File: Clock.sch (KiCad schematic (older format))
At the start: 4 parts, among them Y1 24 MHz

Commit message: First pass at pcb layout
Not really ready to set that in stone, but wanted to get an idea of what size enclosure will work.
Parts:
- C30, C31: footprint (none) -> Capacitor_SMD:C_1210_3225Metric
- R14: footprint (none) -> Resistor_SMD:R_1210_3225Metric
- Y1: footprint (none) -> Crystal:Crystal_SMD_SeikoEpson_MA505-2Pin_12.7x5.1mm
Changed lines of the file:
@@
 $Descr A4 11693 8268
 encoding utf-8
-Sheet 6 6
+Sheet 5 6
 Title ""
 Date ""
@@
 $EndDescr
 $Comp
-L power:GNDREF #PWR?
+L power:GNDREF #PWR0117
 U 1 1 604F5E86
 P 5800 4950
-F 0 "#PWR?" H 5800 4700 50  0001 C CNN
+F 0 "#PWR0117" H 5800 4700 50  0001 C CNN
 F 1 "GNDREF" H 5805 4777 50  0000 C CNN
 F 2 "" H 5800 4950 50  0001 C CNN
@@
 F 0 "C30" H 5515 4596 50  0000 L CNN
 F 1 "18 pF" H 5515 4505 50  0000 L CNN
-F 2 "" H 5438 4400 50  0001 C CNN
+F 2 "Capacitor_SMD:C_1210_3225Metric" H 5438 4400 50  0001 C CNN
 F 3 "~" H 5400 4550 50  0001 C CNN
 	1    5400 4550
@@
 F 0 "C31" H 6265 4596 50  0000 L CNN
 F 1 "18 pF" H 6265 4505 50  0000 L CNN
-F 2 "" H 6188 4400 50  0001 C CNN
+F 2 "Capacitor_SMD:C_1210_3225Metric" H 6188 4400 50  0001 C CNN
 F 3 "~" H 6150 4550 50  0001 C CNN
 	1    6150 4550
@@
 F 0 "Y1" H 5800 4318 50  0000 C CNN
 F 1 "24 MHz" H 5800 4227 50  0000 C CNN
-F 2 "" H 5800 4050 50  0001 C CNN
+F 2 "Crystal:Crystal_SMD_SeikoEpson_MA505-2Pin_12.7x5.1mm" H 5800 4050 50  0001 C CNN
 F 3 "~" H 5800 4050 50  0001 C CNN
 	1    5800 4050
@@
 F 0 "R14" V 5593 3450 50  0000 C CNN
 F 1 "1 MΩ" V 5684 3450 50  0000 C CNN
-F 2 "" V 5730 3450 50  0001 C CNN
+F 2 "Resistor_SMD:R_1210_3225Metric" V 5730 3450 50  0001 C CNN
 F 3 "~" H 5800 3450 50  0001 C CNN
 	1    5800 3450

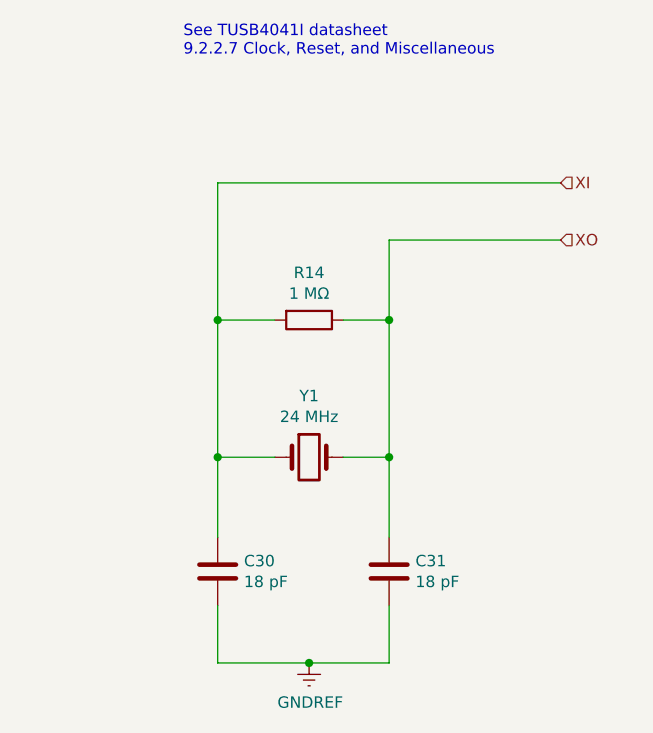
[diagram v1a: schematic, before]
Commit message: Swap TUSB4041I for TUSB2036
The 4041 does more than I need it to, so use the 2036 instead.
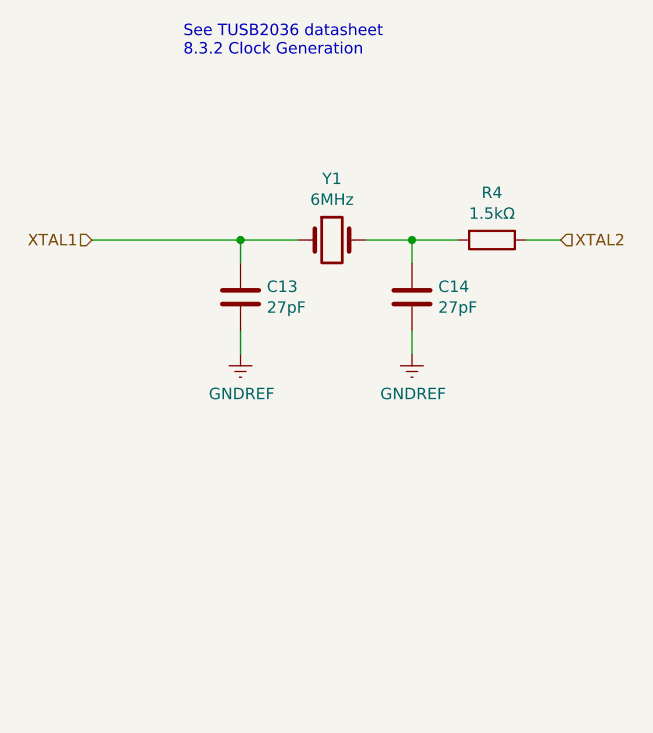
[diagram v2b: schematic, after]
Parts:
- removed C30, C31: 18 pF, Capacitor_SMD:C_1210_3225Metric, symbol Device:C
- removed R14: 1 MΩ, Resistor_SMD:R_1210_3225Metric, symbol Device:R
- added C13, C14: 27pF, Capacitor_SMD:C_1210_3225Metric, symbol Device:C
- added R4: 1.5kΩ, Resistor_SMD:R_1210_3225Metric, symbol Device:R
- Y1: value 24 MHz -> 6MHz; footprint Crystal:Crystal_SMD_SeikoEpson_MA505-2Pin_12.7x5.1mm -> Crystal:Crystal_DS26_D2.0mm_L6.0mm_Horizontal
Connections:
- net GNDREF: now also C13.2, C14.2
- net XI renamed XTAL1
- net XTAL1: now also C13.1
- net XO: no longer names the net of Y1.2
- net XO: now also C14.1, R4.2
- new net XTAL2: R4.1
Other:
- note added: "See TUSB2036 datasheet\n8.3.2 Clock Generation"
- note removed: "See TUSB4041I datasheet\n9.2.2.7 Clock, Reset, and Miscellaneous"
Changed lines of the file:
@@
 $Descr A4 11693 8268
 encoding utf-8
-Sheet 5 6
+Sheet 4 6
 Title ""
 Date ""
@@
 Comment4 ""
 $EndDescr
+Text HLabel 4850 3100 0    50   Input ~ 0
+XTAL1
+Text HLabel 6900 3100 2    50   Input ~ 0
+XTAL2
+Text Notes 5250 2300 0    50   ~ 0
+See TUSB2036 datasheet\n8.3.2 Clock Generation
 $Comp
-L power:GNDREF #PWR0117
-U 1 1 604F5E86
-P 5800 4950
-F 0 "#PWR0117" H 5800 4700 50  0001 C CNN
-F 1 "GNDREF" H 5805 4777 50  0000 C CNN
-F 2 "" H 5800 4950 50  0001 C CNN
-F 3 "" H 5800 4950 50  0001 C CNN
-	1    5800 4950
+L Device:Crystal Y1
+U 1 1 604F9C8F
+P 5900 3100
+F 0 "Y1" H 5900 3368 50  0000 C CNN
+F 1 "6MHz" H 5900 3277 50  0000 C CNN
+F 2 "Crystal:Crystal_DS26_D2.0mm_L6.0mm_Horizontal" H 5900 3100 50  0001 C CNN
+F 3 "~" H 5900 3100 50  0001 C CNN
+	1    5900 3100
+	1    0    0    -1
+$EndComp
+Wire Wire Line
+	4850 3100 5500 3100
+Wire Wire Line
+	6050 3100 6250 3100
+$Comp
+L Device:R R4
+U 1 1 604FA19F
+P 6600 3100
+F 0 "R4" V 6393 3100 50  0000 C CNN
+F 1 "1.5kΩ" V 6484 3100 50  0000 C CNN
+F 2 "Resistor_SMD:R_1210_3225Metric" V 6530 3100 50  0001 C CNN
+F 3 "~" H 6600 3100 50  0001 C CNN
+	1    6600 3100
+	0    1    1    0
+$EndComp
+Wire Wire Line
+	6750 3100 6900 3100
+$Comp
+L Device:C C14
+U 1 1 604FA65B
+P 6250 3350
+F 0 "C14" H 6365 3396 50  0000 L CNN
+F 1 "27pF" H 6365 3305 50  0000 L CNN
+F 2 "Capacitor_SMD:C_1210_3225Metric" H 6288 3200 50  0001 C CNN
+F 3 "~" H 6250 3350 50  0001 C CNN
+	1    6250 3350
 	1    0    0    -1
 $EndComp
 $Comp
-L Device:C C30
-U 1 1 604F6174
-P 5400 4550
-F 0 "C30" H 5515 4596 50  0000 L CNN
-F 1 "18 pF" H 5515 4505 50  0000 L CNN
-F 2 "Capacitor_SMD:C_1210_3225Metric" H 5438 4400 50  0001 C CNN
-F 3 "~" H 5400 4550 50  0001 C CNN
-	1    5400 4550
+L Device:C C13
+U 1 1 604FA9C5
+P 5500 3350
+F 0 "C13" H 5615 3396 50  0000 L CNN
+F 1 "27pF" H 5615 3305 50  0000 L CNN
+F 2 "Capacitor_SMD:C_1210_3225Metric" H 5538 3200 50  0001 C CNN
+F 3 "~" H 5500 3350 50  0001 C CNN
+	1    5500 3350
 	1    0    0    -1
 $EndComp
 $Comp
-L Device:C C31
-U 1 1 604F6998
-P 6150 4550
-F 0 "C31" H 6265 4596 50  0000 L CNN
-F 1 "18 pF" H 6265 4505 50  0000 L CNN
-F 2 "Capacitor_SMD:C_1210_3225Metric" H 6188 4400 50  0001 C CNN
-F 3 "~" H 6150 4550 50  0001 C CNN
-	1    6150 4550
+L power:GNDREF #PWR0135
+U 1 1 604FAB4A
+P 5500 3600
+F 0 "#PWR0135" H 5500 3350 50  0001 C CNN
+F 1 "GNDREF" H 5505 3427 50  0000 C CNN
+F 2 "" H 5500 3600 50  0001 C CNN
+F 3 "" H 5500 3600 50  0001 C CNN
+	1    5500 3600
 	1    0    0    -1
 $EndComp
 $Comp
-L Device:Crystal Y1
-U 1 1 604F8137
-P 5800 4050
-F 0 "Y1" H 5800 4318 50  0000 C CNN
-F 1 "24 MHz" H 5800 4227 50  0000 C CNN
-F 2 "Crystal:Crystal_SMD_SeikoEpson_MA505-2Pin_12.7x5.1mm" H 5800 4050 50  0001 C CNN
-F 3 "~" H 5800 4050 50  0001 C CNN
-	1    5800 4050
+L power:GNDREF #PWR0136
+U 1 1 604FADB7
+P 6250 3600
+F 0 "#PWR0136" H 6250 3350 50  0001 C CNN
+F 1 "GNDREF" H 6255 3427 50  0000 C CNN
+F 2 "" H 6250 3600 50  0001 C CNN
+F 3 "" H 6250 3600 50  0001 C CNN
+	1    6250 3600
 	1    0    0    -1
 $EndComp
-$Comp
-L Device:R R14
-U 1 1 604F8499
-P 5800 3450
-F 0 "R14" V 5593 3450 50  0000 C CNN
-F 1 "1 MΩ" V 5684 3450 50  0000 C CNN
-F 2 "Resistor_SMD:R_1210_3225Metric" V 5730 3450 50  0001 C CNN
-F 3 "~" H 5800 3450 50  0001 C CNN
-	1    5800 3450
-	0    1    1    0
-$EndComp
-Text HLabel 6900 2850 2    50   Input ~ 0
-XI
-Text HLabel 6900 3100 2    50   Input ~ 0
-XO
 Wire Wire Line
-	6900 2850 5400 2850
+	5500 3200 5500 3100
+Connection ~ 5500 3100
 Wire Wire Line
-	5400 2850 5400 3450
+	5500 3100 5750 3100
 Wire Wire Line
-	5650 3450 5400 3450
-Connection ~ 5400 3450
+	6250 3200 6250 3100
+Connection ~ 6250 3100
 Wire Wire Line
-	5400 3450 5400 4050
+	6250 3100 6450 3100
 Wire Wire Line
-	5650 4050 5400 4050
-Connection ~ 5400 4050
+	5500 3500 5500 3600
 Wire Wire Line
-	5400 4050 5400 4400
-Wire Wire Line
-	6900 3100 6150 3100
-Wire Wire Line
-	6150 3100 6150 3450
-Wire Wire Line
-	5950 3450 6150 3450
-Connection ~ 6150 3450
-Wire Wire Line
-	6150 3450 6150 4050
-Wire Wire Line
-	5950 4050 6150 4050
-Connection ~ 6150 4050
-Wire Wire Line
-	6150 4050 6150 4400
-Wire Wire Line
-	5400 4700 5400 4950
-Wire Wire Line
-	5400 4950 5800 4950
-Wire Wire Line
-	6150 4700 6150 4950
-Wire Wire Line
-	6150 4950 5800 4950
-Connection ~ 5800 4950
-Text Notes 5250 2300 0    50   ~ 0
-See TUSB4041I datasheet\n9.2.2.7 Clock, Reset, and Miscellaneous
+	6250 3500 6250 3600
 $EndSCHEMATC

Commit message: Add BOM and clarify some footprints
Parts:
- C13, C14: Manufacturer_Name (none) -> AVX; Manufacturer_Part_Number (none) -> 12102U270JAT2A; Price (none) -> 0.7; Vendor (none) -> Mouser; Vendor Part Number (none) -> 581-12102U270JAT2A
- R4: Manufacturer_Name (none) -> Yageo; Manufacturer_Part_Number (none) -> AC1210FR-071K5L; Price (none) -> 0.31; Vendor (none) -> Mouser; Vendor Part Number (none) -> 603-AC1210FR-071K5L
- Y1: footprint Crystal:Crystal_DS26_D2.0mm_L6.0mm_Horizontal -> Crystal:Crystal_SMD_Abracon_ABM7-2Pin_6.0x3.5mm; Description (none) -> Hub controller clock; Manufacturer_Name (none) -> ABRACON; Manufacturer_Part_Number (none) -> AWSCR-6.00CPLA-C30-T4; Price (none) -> 0.36; Vendor (none) -> Mouser; Vendor Part Number (none) -> 815-CR-6.00CPLA-30-T
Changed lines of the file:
@@
 Comment4 ""
 $EndDescr
-Text HLabel 4850 3100 0    50   Input ~ 0
-XTAL1
-Text HLabel 6900 3100 2    50   Input ~ 0
-XTAL2
-Text Notes 5250 2300 0    50   ~ 0
-See TUSB2036 datasheet\n8.3.2 Clock Generation
 $Comp
 L Device:Crystal Y1
@@
 F 0 "Y1" H 5900 3368 50  0000 C CNN
 F 1 "6MHz" H 5900 3277 50  0000 C CNN
-F 2 "Crystal:Crystal_DS26_D2.0mm_L6.0mm_Horizontal" H 5900 3100 50  0001 C CNN
-F 3 "~" H 5900 3100 50  0001 C CNN
+F 2 "Crystal:Crystal_SMD_Abracon_ABM7-2Pin_6.0x3.5mm" H 5900 3100 50  0001 C CNN
+F 3 "https://www.mouser.com/datasheet/2/3/AWSCR-CPLA-1595603.pdf" H 5900 3100 50  0001 C CNN
+F 4 "Hub controller clock" H 5900 3468 50  0001 C CNN "Description"
+F 5 "ABRACON" H 5900 3468 50  0001 C CNN "Manufacturer_Name"
+F 6 "AWSCR-6.00CPLA-C30-T4" H 5900 3468 50  0001 C CNN "Manufacturer_Part_Number"
+F 7 "0.36" H 5900 3468 50  0001 C CNN "Price"
+F 8 "815-CR-6.00CPLA-30-T" H 5900 3468 50  0001 C CNN "Vendor Part Number"
+F 9 "Mouser" H 5900 3468 50  0001 C CNN "Vendor"
 	1    5900 3100
 	1    0    0    -1
 $EndComp
-Wire Wire Line
-	4850 3100 5500 3100
-Wire Wire Line
-	6050 3100 6250 3100
 $Comp
 L Device:R R4
@@
 F 1 "1.5kΩ" V 6484 3100 50  0000 C CNN
 F 2 "Resistor_SMD:R_1210_3225Metric" V 6530 3100 50  0001 C CNN
-F 3 "~" H 6600 3100 50  0001 C CNN
+F 3 "https://www.mouser.com/datasheet/2/447/PYu_AC_51_RoHS_L_7-1714230.pdf" H 6600 3100 50  0001 C CNN
+F 4 "Yageo" H 6393 3200 50  0001 C CNN "Manufacturer_Name"
+F 5 "AC1210FR-071K5L" H 6393 3200 50  0001 C CNN "Manufacturer_Part_Number"
+F 6 "0.31" H 6393 3200 50  0001 C CNN "Price"
+F 7 "603-AC1210FR-071K5L" H 6393 3200 50  0001 C CNN "Vendor Part Number"
+F 8 "Mouser" H 6393 3200 50  0001 C CNN "Vendor"
 	1    6600 3100
 	0    1    1    0
 $EndComp
-Wire Wire Line
-	6750 3100 6900 3100
 $Comp
 L Device:C C14
@@
 F 1 "27pF" H 6365 3305 50  0000 L CNN
 F 2 "Capacitor_SMD:C_1210_3225Metric" H 6288 3200 50  0001 C CNN
-F 3 "~" H 6250 3350 50  0001 C CNN
+F 3 "https://www.mouser.com/datasheet/2/40/U_Series-894201.pdf" H 6250 3350 50  0001 C CNN
+F 4 "AVX" H 6365 3496 50  0001 C CNN "Manufacturer_Name"
+F 5 "12102U270JAT2A" H 6365 3496 50  0001 C CNN "Manufacturer_Part_Number"
+F 6 "0.7" H 6365 3496 50  0001 C CNN "Price"
+F 7 "581-12102U270JAT2A" H 6365 3496 50  0001 C CNN "Vendor Part Number"
+F 8 "Mouser" H 6365 3496 50  0001 C CNN "Vendor"
 	1    6250 3350
 	1    0    0    -1
@@
 F 1 "27pF" H 5615 3305 50  0000 L CNN
 F 2 "Capacitor_SMD:C_1210_3225Metric" H 5538 3200 50  0001 C CNN
-F 3 "~" H 5500 3350 50  0001 C CNN
+F 3 "https://www.mouser.com/datasheet/2/40/U_Series-894201.pdf" H 5500 3350 50  0001 C CNN
+F 4 "AVX" H 5615 3496 50  0001 C CNN "Manufacturer_Name"
+F 5 "12102U270JAT2A" H 5615 3496 50  0001 C CNN "Manufacturer_Part_Number"
+F 6 "0.7" H 5615 3496 50  0001 C CNN "Price"
+F 7 "581-12102U270JAT2A" H 5615 3496 50  0001 C CNN "Vendor Part Number"
+F 8 "Mouser" H 5615 3496 50  0001 C CNN "Vendor"
 	1    5500 3350
 	1    0    0    -1
@@
 	1    0    0    -1
 $EndComp
+Text HLabel 4850 3100 0    50   Input ~ 0
+XTAL1
+Text HLabel 6900 3100 2    50   Input ~ 0
+XTAL2
+Text Notes 5250 2300 0    50   ~ 0
+See TUSB2036 datasheet\n8.3.2 Clock Generation
+Wire Wire Line
+	4850 3100 5500 3100
+Wire Wire Line
+	6050 3100 6250 3100
+Wire Wire Line
+	6750 3100 6900 3100
 Wire Wire Line
 	5500 3200 5500 3100
-Connection ~ 5500 3100
 Wire Wire Line
 	5500 3100 5750 3100
 Wire Wire Line
 	6250 3200 6250 3100
-Connection ~ 6250 3100
 Wire Wire Line
 	6250 3100 6450 3100
@@
 Wire Wire Line
 	6250 3500 6250 3600
+Connection ~ 5500 3100
+Connection ~ 6250 3100
 $EndSCHEMATC
